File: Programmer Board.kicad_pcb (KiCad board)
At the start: 2 copper layers, 63 x 96 mm, 48 parts, among them J1 105-1103-001, J10 Conn_01x03, J11 105-1102-001, J12 105-1103-001, J13 Conn_01x02, J2 Conn_01x03, J3 105-1102-001, J4 UJ2-MIBH-4-SMT-TR, J5 5-5530843-4, J6 Conn_01x03, J7 302-S101, J9 Conn_02x18_Odd_Even, U1 FT2232D-REEL, U2 TEC2-1219WI, U3 TPS25921x, Y1 CSTNR6M00GH5C000R0

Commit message: Final updates to REV B
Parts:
- J5: value 5-5530843-4 -> EBC20DRAS; footprint Connector_PinHeader_2.54mm:PinHeader_2x20_P2.54mm_Vertical -> LMS-6_Interface_Board:EBC20DRAS; moved to F.Cu
- moved J9 70.6 mm to (177.5, 92.8), turned to 0 degrees
- moved J5 35.2 mm to (147.5, 158.2), turned to 180 degrees
- moved G*** 8.59 mm to (147.5, 118.2)
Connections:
- J9 pad 1: /Card Edge Conn/U3.18 -> /Card Edge Conn/U21.20-DCLK
- J9 pad 11: /Card Edge Conn/HEADER1.7 -> /Card Edge Conn/SW1.2
- J9 pad 13: /Card Edge Conn/U22.3 -> /Card Edge Conn/HEADER1.2
- J9 pad 15: /Card Edge Conn/HEADER1.4 -> /Card Edge Conn/HEADER1.3
- J9 pad 17: /Card Edge Conn/HEADER1.6 -> /Card Edge Conn/HEADER1.5
- J9 pad 19: /Card Edge Conn/HEADER1.5 -> /Card Edge Conn/HEADER1.4
- J9 pad 21: /Card Edge Conn/HEADER1.3 -> /Card Edge Conn/HEADER1.6
- J9 pad 23: /Card Edge Conn/HEADER1.2 -> /Card Edge Conn/U22.3
- J9 pad 25: /Card Edge Conn/SW1.1 -> /Card Edge Conn/HEADER1.7
- J9 pad 27: /Card Edge Conn/SW1.2 -> /Card Edge Conn/J5.3
- J9 pad 29: /Card Edge Conn/SW1.4 -> /Card Edge Conn/SW1.3
- J9 pad 3: /Card Edge Conn/HEADER1.10 -> /Card Edge Conn/J5.2
- J9 pad 31: /Card Edge Conn/HEADER1.1 -> /Card Edge Conn/HEADER1.9
- J9 pad 33: /Card Edge Conn/U21.20-DCLK -> /Card Edge Conn/U3.18
- J9 pad 35: /Card Edge Conn/J5.2 -> /Card Edge Conn/HEADER1.10
- J9 pad 5: /Card Edge Conn/SW1.3 -> /Card Edge Conn/HEADER1.1
- J9 pad 7: /Card Edge Conn/HEADER1.9 -> /Card Edge Conn/SW1.4
- J9 pad 9: /Card Edge Conn/J5.3 -> /Card Edge Conn/SW1.1
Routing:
- net /Card Edge Conn/J5.2: track 13.0 -> 115.8 mm
- net /Card Edge Conn/SW1.4: track 11.8 -> 107.1 mm
- net /Card Edge Conn/U21.20-DCLK: track 9.38 -> 98.4 mm
- net /Card Edge Conn/SW1.2: track 11.9 -> 96.9 mm
- net /Card Edge Conn/HEADER1.1: track 9.38 -> 91.1 mm
- net /Card Edge Conn/SW1.1: track 8.33 -> 81.3 mm
- net /Card Edge Conn/HEADER1.5: track 11.9 -> 77.0 mm
- net /Card Edge Conn/HEADER1.2: track 9.38 -> 71.6 mm
- net /Card Edge Conn/HEADER1.3: track 9.38 -> 66.9 mm
- net /Card Edge Conn/HEADER1.6: track 11.9 -> 68.4 mm
- net /Card Edge Conn/HEADER1.4: track 8.33 -> 57.1 mm
- net /Card Edge Conn/HEADER1.7: track 11.9 -> 60.1 mm
- net /Card Edge Conn/U22.3: track 8.33 -> 49.9 mm
- net /Card Edge Conn/J5.3: track 9.38 -> 42.6 mm
- net /Card Edge Conn/SW1.3: track 9.38 -> 38.7 mm, vias 0 -> 1
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- removed copper zone on B.Cu, net /USB to UART/+5_USB
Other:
- board size 63 x 96 mm -> 80 x 96 mm
- board text added: "LMS6 INTERFACE REV. B GPL 3.0"
- board text removed: "LMS6 INTERFACE REV. A GPL 3.0"

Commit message: Rev C Board layout
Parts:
- removed C4: 33nF, Capacitor_SMD:C_0805_2012Metric_Pad1.18x1.45mm_HandSolder
- removed C5: 0.1uF, Capacitor_SMD:C_0805_2012Metric_Pad1.18x1.45mm_HandSolder
- removed JP4, JP5: JUMPER-SMT_3_1-NC, Jumpers:SMT-JUMPER_3_1-NC_TRACE_NO-SILK
- removed R10: 143K, Resistor_SMD:R_0805_2012Metric_Pad1.20x1.40mm_HandSolder
- removed R11: 280, Resistor_SMD:R_0805_2012Metric_Pad1.20x1.40mm_HandSolder
- removed R13: 1M, Resistor_SMD:R_0805_2012Metric_Pad1.20x1.40mm_HandSolder
- removed Y1: CSTNR6M00GH5C000R0, LMS-6_Interface_Board:CSTNR_Resonator
- added C1: 0.1uF, Capacitor_SMD:C_0805_2012Metric_Pad1.18x1.45mm_HandSolder, F.Cu at (131.5, 117.8)
- added C2: 0.1uF, Capacitor_SMD:C_0805_2012Metric_Pad1.18x1.45mm_HandSolder, F.Cu at (131.0, 125.3)
- added D4: LG R971-KN-1, LED_SMD:LED_0805_2012Metric_Pad1.15x1.40mm_HandSolder, F.Cu at (134.5, 96.2)
- added D5: LG R971-KN-1, LED_SMD:LED_0805_2012Metric_Pad1.15x1.40mm_HandSolder, F.Cu at (134.5, 92.8)
- added D6: LG R971-KN-1, LED_SMD:LED_0805_2012Metric_Pad1.15x1.40mm_HandSolder, F.Cu at (136.0, 121.2)
- added F1: 750mA, Resistor_SMD:R_1812_4532Metric_Pad1.30x3.40mm_HandSolder, B.Cu at (123.0, 87.2)
- added F2: 750mA, Resistor_SMD:R_1812_4532Metric_Pad1.30x3.40mm_HandSolder, B.Cu at (168.5, 87.2)
- added F3: 750 mA, Resistor_SMD:R_1812_4532Metric_Pad1.30x3.40mm_HandSolder, F.Cu at (121.5, 93.8)
- added F4: 750 mA, Resistor_SMD:R_1812_4532Metric_Pad1.30x3.40mm_HandSolder, F.Cu at (121.5, 113.8)
- added FB3: MPZ2012S601AT000, digikey-footprints:0805, F.Cu at (114.5, 123.2)
- added FB4: MPZ2012S601AT000, digikey-footprints:0805, F.Cu at (127.0, 113.8)
- added J1: Conn_01x06, Connector_PinHeader_2.54mm:PinHeader_1x06_P2.54mm_Vertical, F.Cu at (134.5, 113.8)
- added J3: UJ2-MIBH-4-SMT-TR, digikey-footprints:USB_Micro_B_Male_UJ2-MIBH-4-SMT-TR, F.Cu at (107.5, 117.2)
- added J8: Conn_01x06, Connector_PinHeader_2.54mm:PinHeader_1x06_P2.54mm_Vertical, F.Cu at (134.5, 134.2)
- added JP3: JUMPER-SMT_3_1-NC, Jumpers:SMT-JUMPER_3_1-NC_TRACE_NO-SILK, B.Cu at (146.0, 138.8)
- C10: value DNP -> 10uF; footprint Capacitor_SMD:C_0805_2012Metric_Pad1.18x1.45mm_HandSolder -> Capacitor_Tantalum_SMD:CP_EIA-3216-10_Kemet-I_Pad1.58x1.35mm_HandSolder; moved to F.Cu
- D1: value LH_R974-LP-1 -> LG R971-KN-1; footprint digikey-footprints:0805 -> LED_SMD:LED_0805_2012Metric_Pad1.15x1.40mm_HandSolder
- D2, D3: footprint digikey-footprints:0805 -> LED_SMD:LED_0805_2012Metric_Pad1.15x1.40mm_HandSolder
- E1: renamed from J3; value 105-1102-001 -> 575-4; footprint digikey-footprints:Test_Jack_Horiz -> LMS-6_Interface_Board:575_Banana_Jack
- E2: renamed from J1; value 105-1103-001 -> 575-4; footprint digikey-footprints:Test_Jack_Horiz -> LMS-6_Interface_Board:575_Banana_Jack
- E3: renamed from J11; value 105-1102-001 -> 575-4; footprint digikey-footprints:Test_Jack_Horiz -> LMS-6_Interface_Board:575_Banana_Jack
- E4: renamed from J12; value 105-1103-001 -> 575-4; footprint digikey-footprints:Test_Jack_Horiz -> LMS-6_Interface_Board:575_Banana_Jack
- J7: footprint digikey-footprints:PinHeader_2x5_P2.54mm_Drill1.2mm -> digikey-footprints:PinHeader_2x5_P2.54mm_Drill1.02mm
- R3: value 1.5K -> 280
- R4: value 10k -> 280
- R5: value 470 -> 280
- R6: value 470K -> 27; moved to F.Cu
- R7: value 137K -> 280; moved to F.Cu
- R8: value 54.9K -> 27; moved to F.Cu
- R9: value 1.62K -> 280; moved to F.Cu
- U1: value FT2232D-REEL -> FT232RL-REEL; footprint LMS-6_Interface_Board:LQFP-48_7x7mm_Narrow_Pad -> digikey-footprints:SSOP-28_W5.30mm; moved to B.Cu
- U3: value TPS25921x -> FT232RL-REEL; footprint LMS-6_Interface_Board:SOIC-8_W5.4mm -> digikey-footprints:SSOP-28_W5.30mm
- moved R8 41.5 mm to (124.0, 117.8), turned to 180 degrees
- moved D1 40.9 mm to (136.0, 124.8)
- moved R5 38.3 mm to (139.5, 92.8), turned to 180 degrees
- moved R9 36.7 mm to (154.2, 125.8)
- moved C10 36.2 mm to (134.4, 130.8), turned to 180 degrees
- moved R2 35.9 mm to (124.0, 97.8)
- moved C6 35.6 mm to (129.5, 104.2)
- moved U3 35.2 mm to (134.0, 124.8), turned to 180 degrees
- moved R3 34.0 mm to (139.5, 96.2)
- moved R6 33.3 mm to (124.0, 120.2), turned to 180 degrees
- moved C7 33.3 mm to (130.0, 109.2), turned to 180 degrees
- moved R1 31.6 mm to (124.0, 100.2)
- moved R7 29.8 mm to (141.0, 121.2), turned to 180 degrees
- moved E4 29.2 mm to (177.5, 79.2)
- moved U1 28.6 mm to (132.5, 103.8), turned to 180 degrees
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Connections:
- net Net-(FB1-Pad1) renamed /USB to UART1/SH_GND
- C10 pad 1: Net-(C10-Pad1) -> /+5_USB
- C3 pad 1: Net-(C3-Pad1) -> /+5_USB
- C6 pad 1: /USB to UART/+5_USB -> /USB to UART1/3V3OUT
- C7 pad 1: /USB to UART/+5_USB -> /+5_USB
- D1 pad 1: /eFuse/eFuse_In -> /sheet5FC8868D/TXLED
- D2 pad 1: /USB to UART/+5_USB -> Net-(D2-Pad1)
- D2 pad 2: Net-(D2-Pad2) -> /+5_USB
- E1 pad 1: /+PS -> Net-(E1-Pad1)
- E3 pad 1: Net-(J10-Pad1) -> Net-(E3-Pad1)
- FB2 pad 1: Net-(FB2-Pad1) -> Net-(F3-Pad1)
- FB2 pad 2: /USB to UART/+5_USB -> /+5_USB
- J10 pad 1: Net-(J10-Pad1) -> Net-(F2-Pad1)
- J13 pad 2: Net-(D3-Pad1) -> Net-(D3-Pad2)
- J2 pad 2: /eFuse/eFuse_In -> /DC-DC Converter/+V_in
- J2 pad 3: /USB to UART/+5_USB -> /+5_USB
- J4 pad 1: Net-(FB2-Pad1) -> Net-(F3-Pad2)
- J4 pad 2: /USB to UART/IN_USBD_P -> /USB to UART1/IN_USBD_N
- J4 pad 3: /USB to UART/IN_USBD_N -> /USB to UART1/IN_USBD_P
- R1 pad 1: /USB to UART/USBD_P -> /USB to UART1/USBD_P
- R1 pad 2: /USB to UART/IN_USBD_P -> /USB to UART1/IN_USBD_P
- R12 pad 1: Net-(D3-Pad2) -> Net-(D3-Pad1)
- R2 pad 1: /USB to UART/USBD_N -> /USB to UART1/USBD_N
- R2 pad 2: /USB to UART/IN_USBD_N -> /USB to UART1/IN_USBD_N
- R3 pad 1: /USB to UART/RSTOUT -> /+5_USB
- R3 pad 2: /USB to UART/USBD_P -> Net-(D4-Pad2)
- R4 pad 1: Net-(R4-Pad1) -> /+5_USB
- R4 pad 2: /USB to UART/+5_USB -> Net-(D1-Pad2)
- R5 pad 1: Net-(C3-Pad1) -> /+5_USB
- R5 pad 2: /USB to UART/+5_USB -> Net-(D5-Pad2)
- R6 pad 1: /eFuse/eFuse_In -> /sheet5FC8868D/USBD_P
- R6 pad 2: Net-(R6-Pad2) -> /sheet5FC8868D/IN_USBD_P
- R7 pad 1: Net-(R6-Pad2) -> /+5_USB
- R7 pad 2: Net-(R7-Pad2) -> Net-(D6-Pad2)
- R8 pad 1: Net-(R7-Pad2) -> /sheet5FC8868D/USBD_N
- R8 pad 2: GND -> /sheet5FC8868D/IN_USBD_N
- R9 pad 1: Net-(R9-Pad1) -> Net-(D2-Pad1)
- R9 pad 2: Net-(D1-Pad2) -> GND
- U1 pad 1: (no net) -> /Card Edge Conn/GPS.RXD
- U1 pad 11: (no net) -> /USB to UART1/CTS
- U1 pad 14: /USB to UART/+5_USB -> (no net)
- U1 pad 15: (no net) -> /USB to UART1/USBD_P
- U1 pad 16: (no net) -> /USB to UART1/USBD_N
- U1 pad 17: (no net) -> /USB to UART1/3V3OUT
- U1 pad 2: Net-(R4-Pad1) -> /USB to UART1/DTR
- U1 pad 20: (no net) -> /+5_USB
- U1 pad 21: (no net) -> GND
- U1 pad 22: (no net) -> /USB to UART1/RXLED
- U1 pad 23: /Card Edge Conn/GPS.TXD -> /USB to UART1/TXLED
- U1 pad 24: /Card Edge Conn/GPS.RXD -> (no net)
- U1 pad 26: (no net) -> GND
- U1 pad 3: /USB to UART/+5_USB -> (no net)
- U1 pad 4: /USB to UART/+5_USB -> /+5_USB
- U1 pad 5: /USB to UART/RSTOUT -> /Card Edge Conn/GPS.TXD
- U1 pad 6: /USB to UART/3V3OUT -> (no net)
- U1 pad 7: /USB to UART/USBD_P -> GND
- U1 pad 8: /USB to UART/USBD_N -> (no net)
- U1 pad 9: GND -> (no net)
- U3 pad 1: GND -> /sheet5FC8868D/TXD
- U3 pad 2: Net-(C10-Pad1) -> /sheet5FC8868D/DTR
- U3 pad 3: Net-(R6-Pad2) -> (no net)
- U3 pad 4: /eFuse/eFuse_In -> /+5_USB
- U3 pad 5: /DC-DC Converter/+V_in -> /sheet5FC8868D/RXD
- U3 pad 6: Net-(R9-Pad1) -> (no net)
- U3 pad 7: Net-(R10-Pad1) -> GND
- U3 pad 8: Net-(R7-Pad2) -> (no net)
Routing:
- net /Card Edge Conn/GPS.RXD: track 10.9 -> 66.9 mm
- net Net-(J10-Pad1): track 54.1 -> 0.00 mm
- net /Card Edge Conn/GPS.TXD: track 12.7 -> 62.2 mm, vias 2 -> 0
- net Net-(F2-Pad1): track 0.00 -> 38.9 mm
- net /Card Edge Conn/U3.19: track 56.7 -> 22.1 mm, vias 2 -> 0
- net /USB to UART/UART2.RXD: track 33.7 -> 0.00 mm, vias 2 -> 0
- net /USB to UART/IN_USBD_P: track 32.8 -> 0.00 mm
- net /USB to UART/IN_USBD_N: track 32.8 -> 0.00 mm
- net /USB to UART/+5_USB: track 32.2 -> 0.00 mm, vias 2 -> 0
- net GND: track 33.1 -> 57.4 mm, vias 16 -> 13
- net /sheet5FC8868D/RXD: track 0.00 -> 23.2 mm
- net Net-(R6-Pad2): track 18.4 -> 0.00 mm
- net Net-(C3-Pad1): track 17.8 -> 0.00 mm
- net /Card Edge Conn/ST7-ICCCLK: track 47.2 -> 31.6 mm
- net /sheet5FC8868D/SH_GND: track 0.00 -> 15.2 mm
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- added copper zone on F.Cu, net /+5_USB
- added copper zone on F.Cu, net /USB to UART1/SH_GND
- added copper zone on F.Cu, net /sheet5FC8868D/SH_GND
- removed copper zone on B.Cu, net /DC-DC Converter/+V_in
- removed copper zone on F.Cu, net /DC-DC Converter/+V_in
- removed copper zone on F.Cu, net /USB to UART/+5_USB
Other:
- board text added: "+"
- board text added: "+5V LED"
- board text added: "-"
- board text added: "LMS6 INTERFACE REV. C GPL 3.0"
- board text added: "RX LED"
- board text added: "TX LED"
- board text removed: "LMS6 INTERFACE REV. B GPL 3.0"

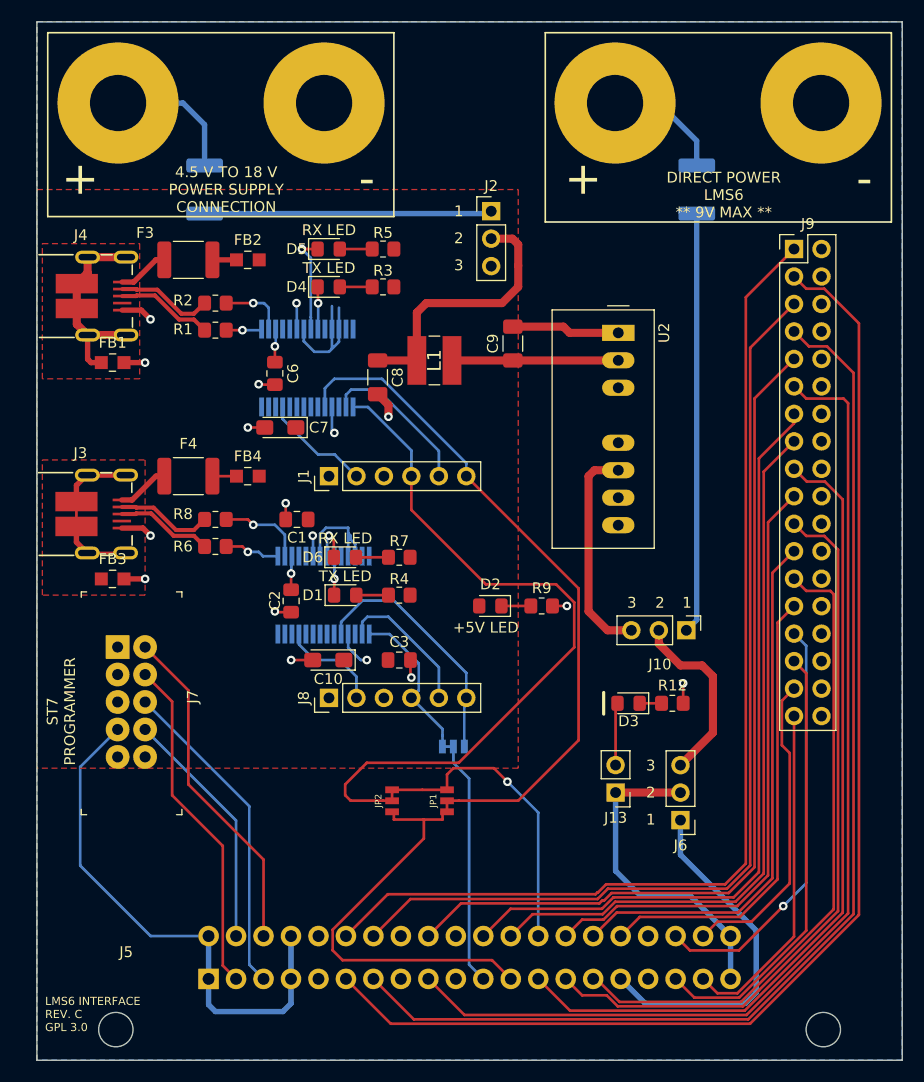
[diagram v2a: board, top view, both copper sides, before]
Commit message: Rev C PCB as sent to fabrication
REV C PCB as sent to fabrication with clean up directory structure.
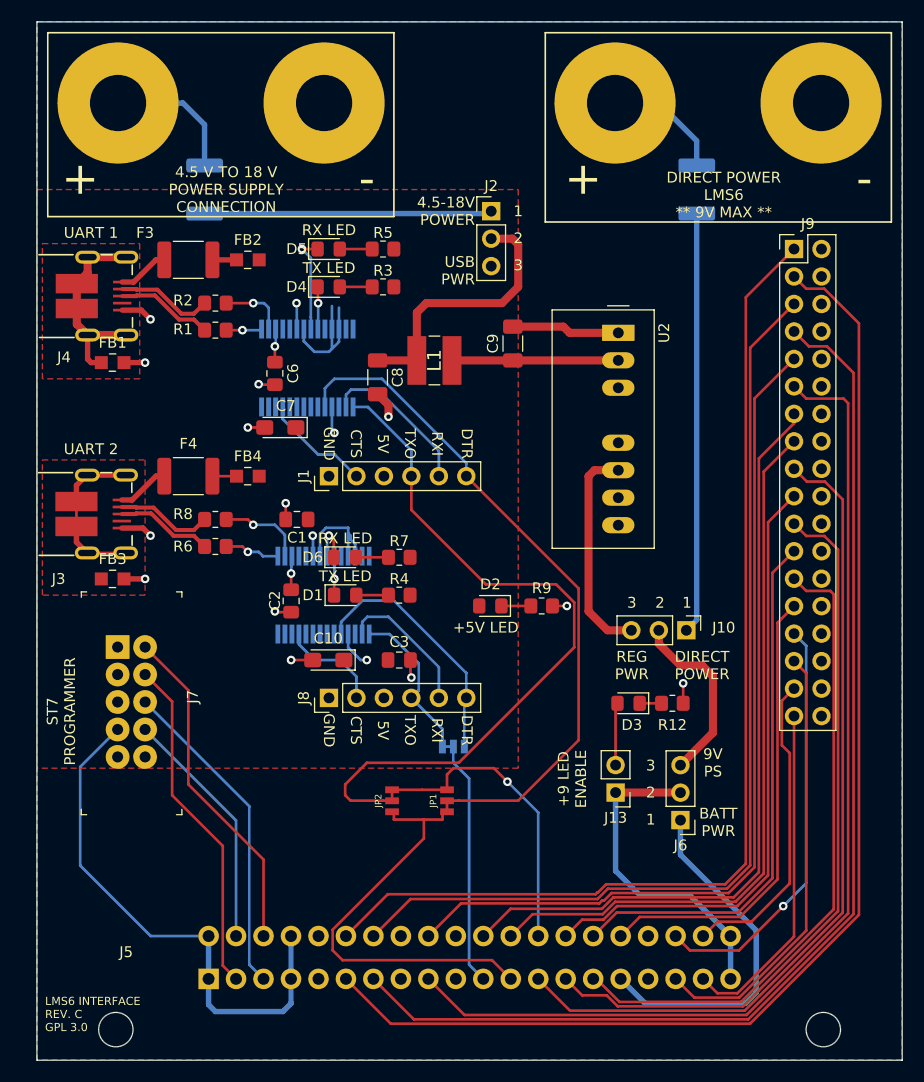
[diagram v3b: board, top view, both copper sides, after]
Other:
- board text added: "+9 LED ENABLE"
- board text added: "4.5-18V POWER"
- board text added: "5V"
- board text added: "9V PS"
- board text added: "BATT PWR"
- board text added: "CTS"
- board text added: "DIRECT POWER"
- board text added: "DTR"
- board text added: "GND"
- board text added: "REG PWR"
- board text added: "RXI"
- board text added: "TXO"
- board text added: "UART 1"
- board text added: "UART 2"
- board text added: "USB PWR"
